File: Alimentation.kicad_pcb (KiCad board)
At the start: 2 copper layers, 50 x 50 mm, 29 parts, among them P1 Prise_Equilibrage, P10 CONN_01X02, P2 Prise_Alim, P3 Prise_Batterie, P4 ConnecteurBippeur, P5 CONN_01X04, P6 CAN_conn, P7 CAN_conn, P8 CONN_01X02, P9 CONN_01X02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

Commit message: retourné connecteur CAN
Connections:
- P6 pad 1: +9V -> GND
- P6 pad 4: GND -> +9V
- P7 pad 1: +9V -> GND
- P7 pad 4: GND -> +9V
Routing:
- net GND: track 184.8 -> 167.8 mm
- net +9V: track 81.0 -> 85.6 mm

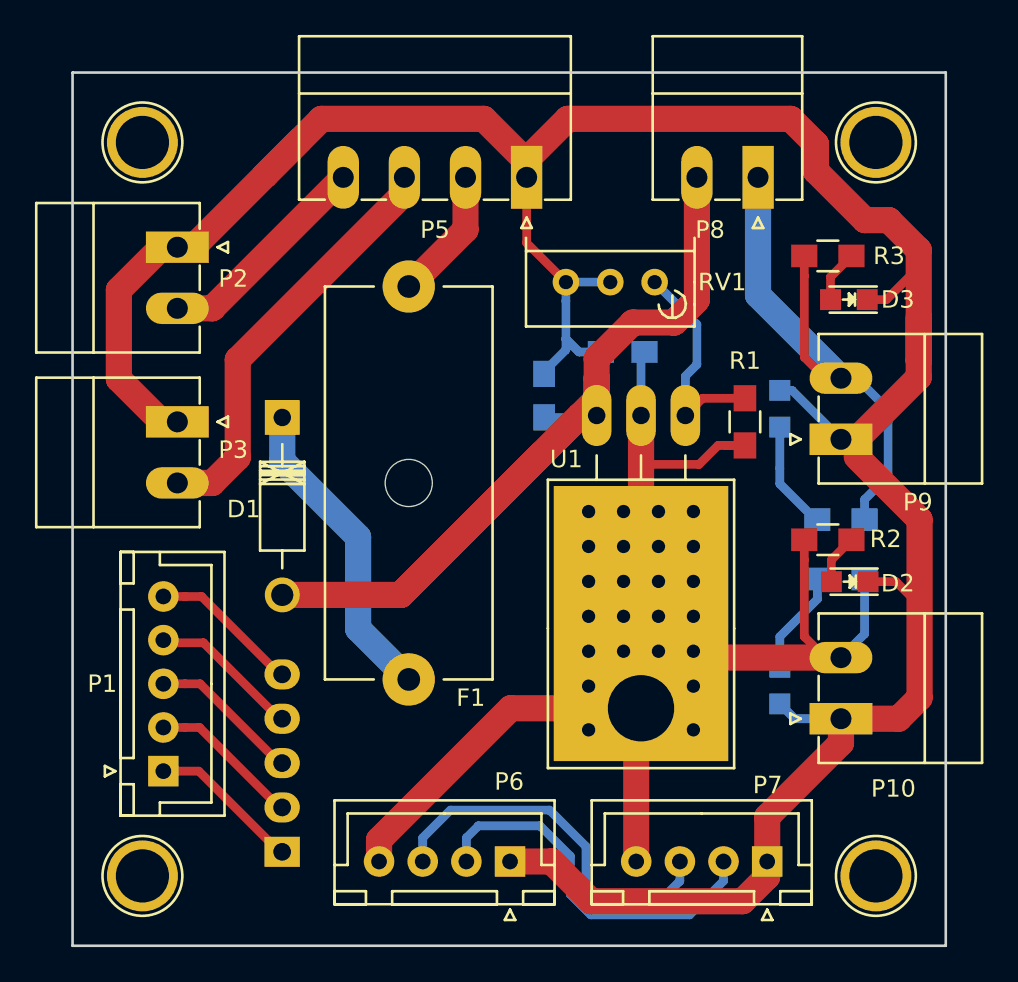
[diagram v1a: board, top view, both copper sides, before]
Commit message: ajoute des vias entre les deux plans de masse
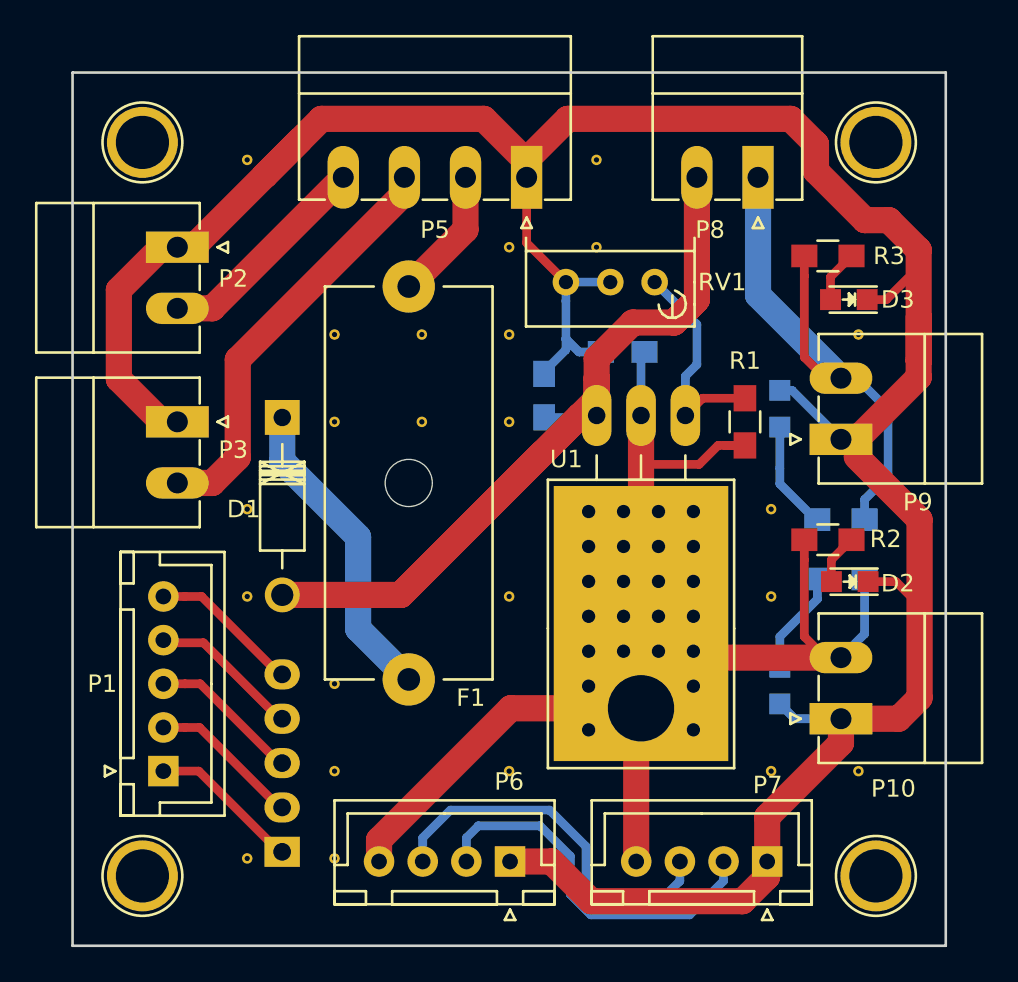
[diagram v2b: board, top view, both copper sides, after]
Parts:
- added REF**: Via, PhoenixRobotik:Via-0.6mm, F.Cu at (115.0, 95.0)
- added REF**: Via, PhoenixRobotik:Via-0.6mm, F.Cu at (110.0, 80.0)
- added REF**: Via, PhoenixRobotik:Via-0.6mm, F.Cu at (140.0, 75.0)
- added REF**: Via, PhoenixRobotik:Via-0.6mm, F.Cu at (110.0, 75.0)
- added REF**: Via, PhoenixRobotik:Via-0.6mm, F.Cu at (125.0, 70.0)
- added REF**: Via, PhoenixRobotik:Via-0.6mm, F.Cu at (120.0, 70.0)
- added REF**: Via, PhoenixRobotik:Via-0.6mm, F.Cu at (115.0, 70.0)
- added REF**: Via, PhoenixRobotik:Via-0.6mm, F.Cu at (145.0, 65.0)
- added REF**: Via, PhoenixRobotik:Via-0.6mm, F.Cu at (125.0, 65.0)
- added REF**: Via, PhoenixRobotik:Via-0.6mm, F.Cu at (120.0, 65.0)
- added REF**: Via, PhoenixRobotik:Via-0.6mm, F.Cu at (115.0, 65.0)
- added REF**: Via, PhoenixRobotik:Via-0.6mm, F.Cu at (110.0, 95.0)
- added REF**: Via, PhoenixRobotik:Via-0.6mm, F.Cu at (130.0, 60.0)
- added REF**: Via, PhoenixRobotik:Via-0.6mm, F.Cu at (125.0, 60.0)
- added REF**: Via, PhoenixRobotik:Via-0.6mm, F.Cu at (130.0, 55.0)
- added REF**: Via, PhoenixRobotik:Via-0.6mm, F.Cu at (110.0, 55.0)
- added REF**: Via, PhoenixRobotik:Via-0.6mm, F.Cu at (145.0, 90.0)
- added REF**: Via, PhoenixRobotik:Via-0.6mm, F.Cu at (140.0, 90.0)
- added REF**: Via, PhoenixRobotik:Via-0.6mm, F.Cu at (125.0, 90.0)
- added REF**: Via, PhoenixRobotik:Via-0.6mm, F.Cu at (115.0, 90.0)
- added REF**: Via, PhoenixRobotik:Via-0.6mm, F.Cu at (115.0, 85.0)
- added REF**: Via, PhoenixRobotik:Via-0.6mm, F.Cu at (140.0, 80.0)
- added REF**: Via, PhoenixRobotik:Via-0.6mm, F.Cu at (125.0, 80.0)

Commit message: ajout nom, url et export gerber
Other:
- board text added: "Phoenix Robotik - Carte Alim '17"
- board text added: "https://github.com/PhoenixRobotik/alim-elec"
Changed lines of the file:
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@@
     (area 99.924999 49.924999 150.075001 100.075001)
     (thickness 1.6)
-    (drawings 8)
+    (drawings 10)
     (tracks 180)
     (zones 0)
@@
       (net 4 GND) (zone_connect 2))
   )
+  (gr_text https://github.com/PhoenixRobotik/alim-elec (at 125 59.5) (layer B.SilkS)
+    (effects (font (size 0.7 0.7) (thickness 0.175)) (justify mirror))
+  )
+  (gr_text "Phoenix Robotik - Carte Alim '17" (at 124.75 51.75) (layer B.SilkS)
+    (effects (font (size 1.5 1.5) (thickness 0.3)) (justify mirror))
+  )
   (dimension 42 (width 0.3) (layer Dwgs.User)

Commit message: correct OSHW logo
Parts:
- added REF***: OSHW-Logo2_7.3x6mm_SilkScreen, Symbols:OSHW-Logo2_7.3x6mm_SilkScreen, B.Cu at (110.0, 55.5)

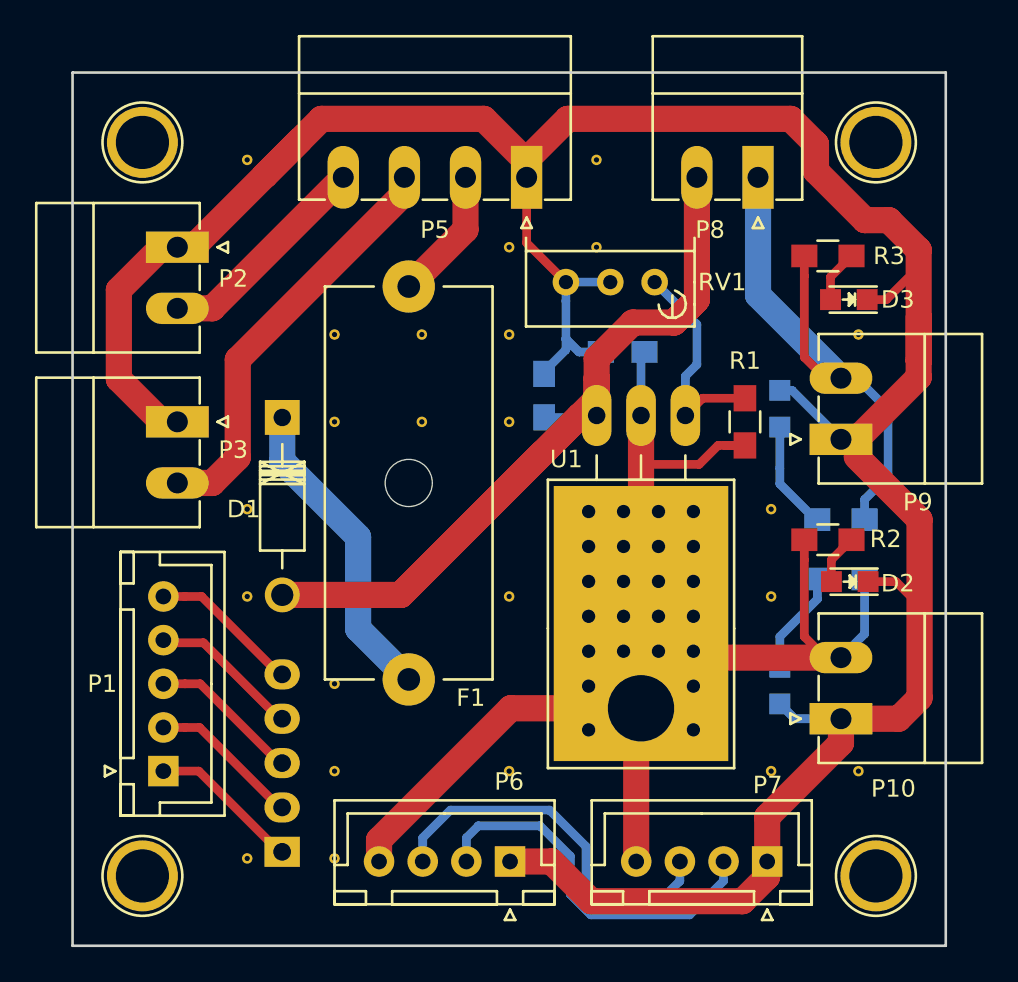
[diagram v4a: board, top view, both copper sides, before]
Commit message: good schottky footprint
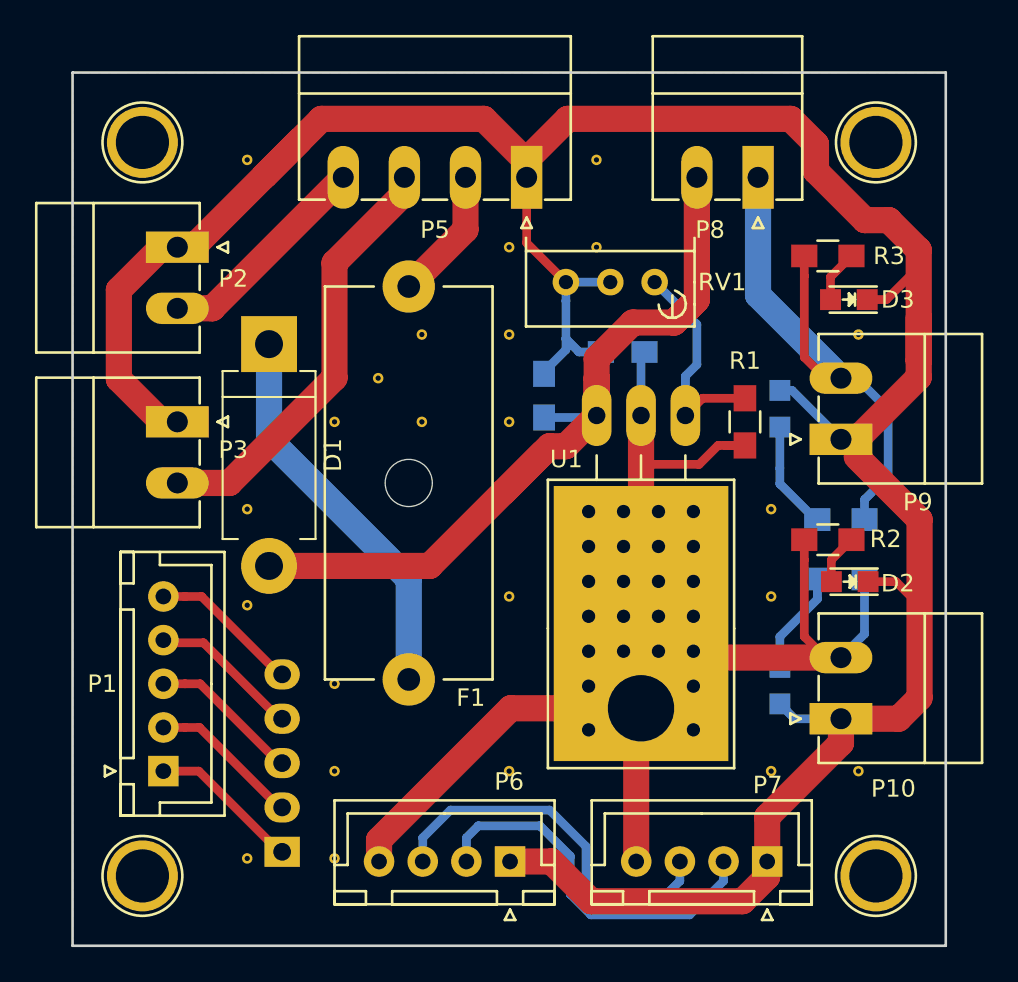
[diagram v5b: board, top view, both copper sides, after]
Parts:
- D1: footprint Diodes_ThroughHole:Diode_DO-41_SOD81_Horizontal_RM10 -> Diodes_THT:D_DO-201AD_P12.70mm_Horizontal
- moved D1 4.27 mm to (111.2, 65.5)
- moved REF** 3.54 mm to (117.5, 67.5)
- moved REF** 0.50 mm to (110.0, 80.5)
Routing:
- net Net-(C1-Pad1): track 73.6 -> 49.4 mm
- net Net-(D1-Pad1): track 18.0 -> 22.5 mm
- net Net-(P3-Pad2): track 24.1 -> 24.6 mm
